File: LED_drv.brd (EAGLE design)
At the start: 160 x 100 mm, 69 parts, among them IC1 LM3409, IC2 LM393D, Q2 IPD50R380, T1 IRLR9343PBF, T2 BCX56, T4 BT169, T5 BT169, T6 TLP266J

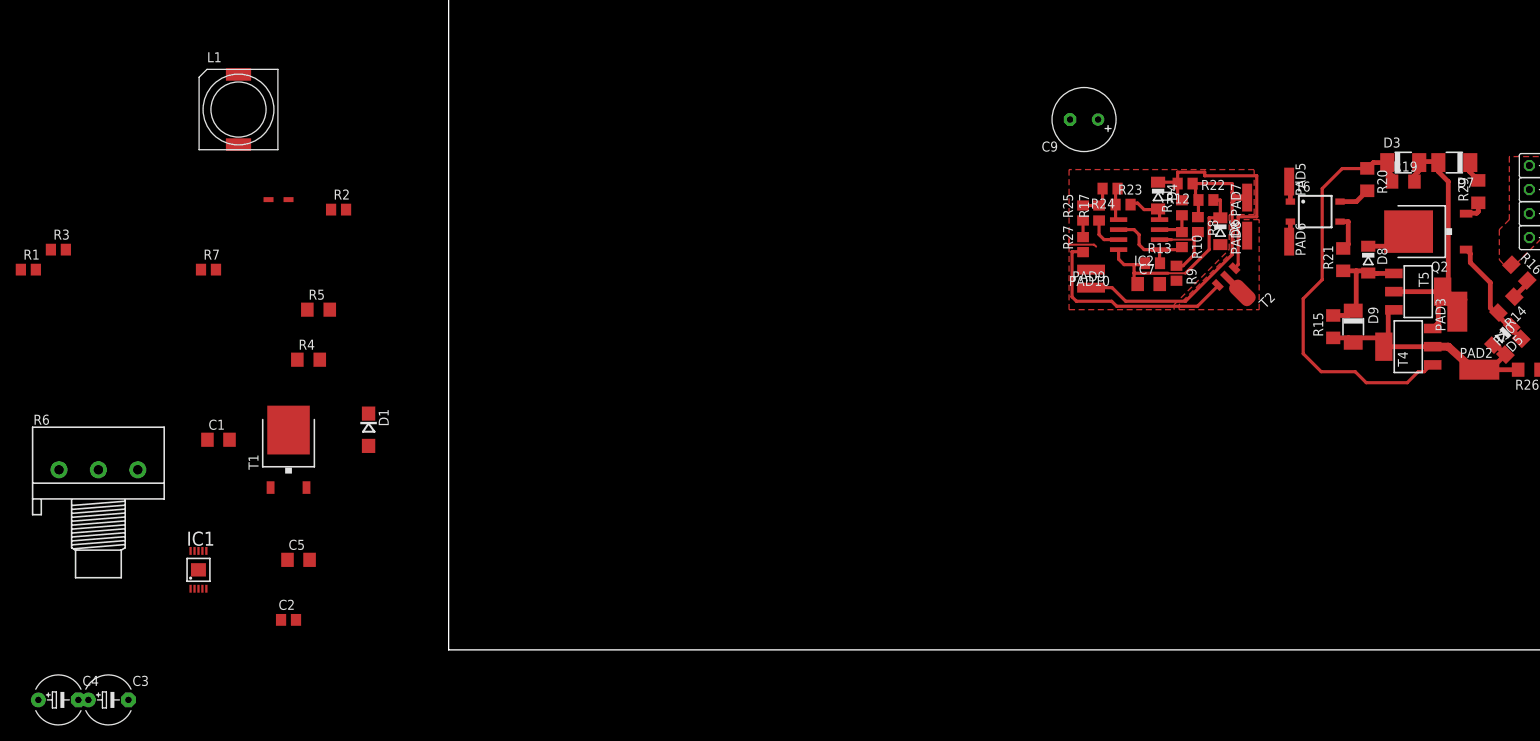
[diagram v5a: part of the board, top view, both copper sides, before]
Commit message: PCB layout complete
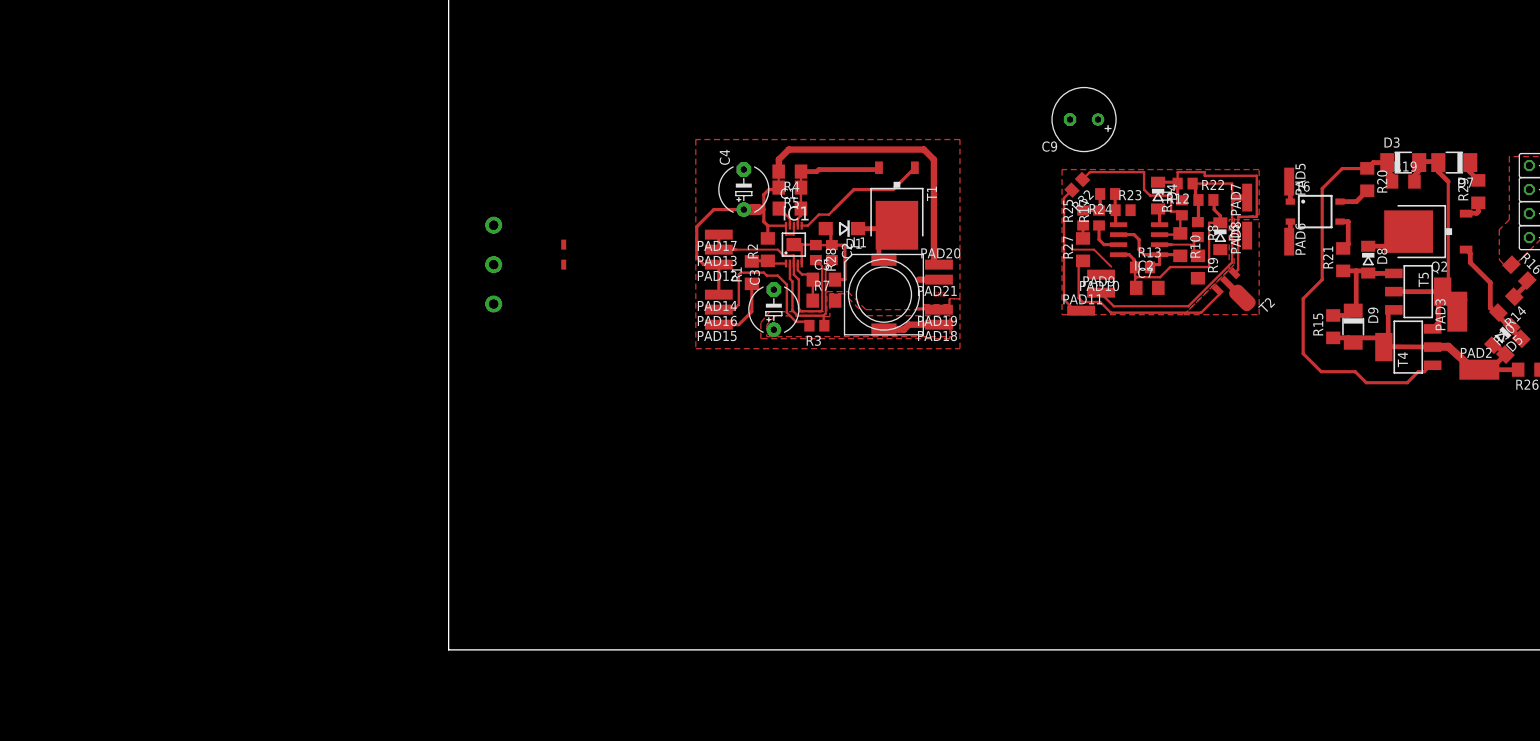
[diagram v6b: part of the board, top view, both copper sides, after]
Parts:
- added PAD11, PAD12, PAD13, PAD14, PAD15, PAD16, PAD17, PAD18, PAD19, PAD20, PAD21: (no value), wirepad:SMD1,27-2,54
- added R28: 1M, rcl:R0805
- added R32: 100k, resistor:R0805
- R1, R2, R7: device rcl:R0805 -> rcl:R1206
- R10: value 150k -> 180k; device resistor:R0805 -> rcl:R1206
- R27, R9: device resistor:R0805 -> rcl:R1206
- moved C4 108.5 mm to (37.5, 58.4), turned to 90 degrees
- moved C3 97.9 mm to (41.3, 43.2), turned to 90 degrees
- moved R3 96.7 mm to (46.7, 41.1), turned to 180 degrees
- moved R1 91.8 mm to (38.5, 47.9), turned to 90 degrees
- moved IC1 86.1 mm to (43.8, 51.4)
- moved L1 85.2 mm to (55.2, 45.1)
- moved C2 83.2 mm to (48.6, 50.4), turned to 270 degrees
- moved T1 83.2 mm to (56.9, 56.4), turned to 180 degrees
- moved C1 78.2 mm to (43.3, 56.0)
- moved R7 78.2 mm to (47.6, 44.3)
- moved C5 75.6 mm to (47.6, 47.0)
- moved R4 65.6 mm to (43.3, 60.7), turned to 180 degrees
- moved D1 65.3 mm to (49.9, 53.5), turned to 180 degrees
- moved R5 61.8 mm to (43.3, 58.7), turned to 180 degrees
- moved R6 56.5 mm to (5.71, 48.9), flipped to the bottom, turned to 90 degrees
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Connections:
- removed net N$11: IC1.3, S1.1
- removed net N$20: IC2.3, R10.1, R11.1
- new net ACTIVATION: IC1.3, PAD11.1, PAD13.1, PAD17.1, R28.2, R32.2, S1.1
- new net EER: IC2.3, R10.1, R11.1, R32.1
- net GND: now also PAD15.1, PAD19.1, PAD21.1, R28.1
- net N$10: now also PAD18.1
- net N$2: now also PAD12.1, PAD14.1, PAD20.1
- net N$8: now also PAD16.1
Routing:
- net N$2: track 0.00 -> 72.2 mm
- net ACTIVATION: track 0.00 -> 45.6 mm
- net GND: track 9.66 -> 40.7 mm
- net EER: track 0.00 -> 23.4 mm
- net N$8: track 0.00 -> 20.5 mm
- net N$5: track 0.00 -> 19.1 mm
- net N$4: track 0.00 -> 18.3 mm
- net N$9: track 0.00 -> 17.4 mm
- net N$6: track 0.00 -> 9.92 mm
- net N$10: track 0.00 -> 7.25 mm
- net N$13: track 0.00 -> 6.33 mm
- net N$20: track 5.29 -> 0.00 mm
- net N$1: track 0.00 -> 4.71 mm
- net N$3: track 0.00 -> 2.83 mm
- net N$19: track 10.3 -> 8.08 mm
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- added copper zone on layer 1, net N$10
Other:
- board text added: "GND"

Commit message: PCB layout complete
minor update
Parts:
- removed C4: 22uF/50V, rcl:E5-6
- removed C6: 100n/400V, rcl:C075-032X103
- added 0R, R31, R33, R34, R35, R36: 1R, resistor:R1206
- added C12, C13: 22uF/50V, rcl:E5-6
- added F1: (no value), fuse:SH22,5A
- added PAD22, PAD23, PAD24, PAD25, PAD26, PAD27, PAD28, PAD29: (no value), wirepad:SMD1,27-2,54
- added R37: S14K275_SMD, varistor:S14K275_SMD
- moved PAD17 36.3 mm to (68.3, 65.3)
- moved PAD19 16.9 mm to (68.3, 58.9)
- moved PAD21 15.7 mm to (68.3, 61.5)
- moved PAD20 15.7 mm to (68.3, 63.4)
- moved PAD18 6.13 mm to (68.3, 40.6)
- moved D2 5.04 mm to (146.4, 35.3), turned to 0 degrees
- moved R2 3.60 mm to (38.1, 53.5), turned to 0 degrees
- moved R30 2.98 mm to (134.7, 41.4), turned to 90 degrees
- moved R16 2.94 mm to (135.5, 50.8), turned to 270 degrees
- moved R14 2.54 mm to (134.2, 46.4), turned to 180 degrees
- moved D5 1.84 mm to (132.7, 41.4), turned to 270 degrees
- moved R26 1.30 mm to (135.9, 35.6)
- moved R18 1.22 mm to (140.9, 35.6)
- moved D1 0.84 mm to (50.7, 53.2)
- moved C2 0.51 mm to (48.6, 49.9)
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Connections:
- new net 230VAC(N/L)_IN: F1.2
- new net N$11: C13.+, C3.+, L1.2, R31.2, R33.2, R34.2, R35.2, R36.2, R7.2
- new net N$20: PAD22.1, R33.1
- new net N$32: PAD18.1, R31.1
- new net N$35: PAD23.1, R34.1
- new net N$36: PAD24.1, R35.1
- new net N$37: PAD25.1, R36.1
- net 230VAC(L/N): now also R37.2
- net 230VAC(N/L): now also F1.1, R37.1
- net ACTIVATION: now also 0R.1; no longer PAD17.1, S1.1
- net GND: now also C12.-, C13.-, PAD26.1, PAD27.1, PAD28.1, PAD29.1; no longer C4.-
- net N$10: now also 0R.2, PAD17.1, S1.1; no longer C3.+, L1.2, PAD18.1, R7.2
- net N$14: no longer C6.1
- net N$2: now also C12.+; no longer C4.+
- net N$34: no longer C6.2
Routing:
- net N$10: track 7.25 -> 33.4 mm
- net N$11: track 0.00 -> 13.3 mm
- net ACTIVATION: track 45.6 -> 55.7 mm
- net 230VAC(L/N): track 7.50 -> 15.7 mm
- net N$1: track 4.71 -> 11.4 mm
- net N$14: track 19.8 -> 25.0 mm
- net N$2: track 72.2 -> 67.8 mm
- net GND: track 40.7 -> 36.9 mm
- net 230VAC(N/L): track 36.4 -> 39.9 mm
- net N$7: track 14.9 -> 11.5 mm
- net N$37: track 0.00 -> 2.77 mm
- net N$36: track 0.00 -> 2.77 mm
- net N$35: track 0.00 -> 2.77 mm
- net N$32: track 0.00 -> 2.77 mm
- net N$20: track 0.00 -> 2.77 mm
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- added copper zone on layer 1, net N$11
- removed copper zone on layer 1, net N$10
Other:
- board text added: "ACT 42V GND"
- board text added: "LED+"
- board text added: "PR"
- board text added: "SW"
- board text removed: "GND"

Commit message: test_release
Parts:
- added D10, D11: 1n4002, diode:DO214AC
- added R38: 51k, rcl:R1206
- added R39: 86k, rcl:R1206
- added R40: 47k, rcl:R0805
- 0R: value 1R -> 0R
- R1: value (none) -> 7k5
- R2: value (none) -> 51k
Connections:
- new net N$40: PAD14.1, R39.1, R6.3
- new net N$41: D10.A, D11.C
- new net N$44: D11.A, R38.1, R39.2
- net GND: now also D10.C
- net N$2: now also R38.2; no longer PAD14.1, R6.3
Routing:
- net N$2: track 67.8 -> 64.0 mm
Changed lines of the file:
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@@
 <layer number="37" name="tTest" color="7" fill="1" visible="no" active="yes"/>
 <layer number="38" name="bTest" color="7" fill="1" visible="no" active="yes"/>
-<layer number="39" name="tKeepout" color="4" fill="11" visible="yes" active="yes"/>
-<layer number="40" name="bKeepout" color="1" fill="11" visible="yes" active="yes"/>
-<layer number="41" name="tRestrict" color="4" fill="10" visible="yes" active="yes"/>
-<layer number="42" name="bRestrict" color="1" fill="10" visible="yes" active="yes"/>
+<layer number="39" name="tKeepout" color="4" fill="11" visible="no" active="yes"/>
+<layer number="40" name="bKeepout" color="1" fill="11" visible="no" active="yes"/>
+<layer number="41" name="tRestrict" color="4" fill="10" visible="no" active="yes"/>
+<layer number="42" name="bRestrict" color="1" fill="10" visible="no" active="yes"/>
 <layer number="43" name="vRestrict" color="2" fill="10" visible="no" active="yes"/>
 <layer number="44" name="Drills" color="7" fill="1" visible="no" active="yes"/>
 <layer number="45" name="Holes" color="7" fill="1" visible="no" active="yes"/>
 <layer number="46" name="Milling" color="3" fill="1" visible="no" active="yes"/>
-<layer number="47" name="Measures" color="7" fill="1" visible="yes" active="yes"/>
-<layer number="48" name="Document" color="7" fill="1" visible="yes" active="yes"/>
+<layer number="47" name="Measures" color="7" fill="1" visible="no" active="yes"/>
+<layer number="48" name="Document" color="7" fill="1" visible="no" active="yes"/>
 <layer number="49" name="Reference" color="7" fill="1" visible="yes" active="yes"/>
 <layer number="51" name="tDocu" color="7" fill="1" visible="yes" active="yes"/>
-<layer number="52" name="bDocu" color="7" fill="1" visible="yes" active="yes"/>
+<layer number="52" name="bDocu" color="7" fill="1" visible="no" active="yes"/>
 <layer number="90" name="Modules" color="5" fill="1" visible="no" active="no"/>
 <layer number="91" name="Nets" color="2" fill="1" visible="no" active="no"/>
@@
 <element name="IC2" library="linear" package="SO08" value="LM393D" x="87.63" y="52.07" rot="R90"/>
 <element name="L1" library="miscrel" package="CDRH104-R" value="CDRH104R" x="55.245" y="45.085"/>
-<element name="R1" library="rcl" package="R1206" value="" x="38.481" y="47.879" rot="R90"/>
+<element name="R1" library="rcl" package="R1206" value="7k5" x="38.481" y="47.879" rot="R90"/>
 <element name="R10" library="rcl" package="R1206" value="180k" x="92.8624" y="51.435" rot="R270"/>
 <element name="R11" library="resistor" package="R0805" value="100k" x="93.0656" y="56.1086" rot="R90"/>
 <element name="R12" library="resistor" package="R0805" value="47k" x="93.472" y="59.182" rot="R180"/>
-<element name="R2" library="rcl" package="R1206" value="" x="38.1" y="53.467"/>
+<element name="R2" library="rcl" package="R1206" value="51k" x="38.1" y="53.467"/>
 <element name="R3" library="rcl" package="R0805" value="1k" x="46.736" y="41.148" rot="R180"/>
 <element name="R4" library="resistor" package="R1206" value="1R" x="43.307" y="60.706" rot="R180"/>
@@
 <element name="C12" library="rcl" package="E5-6" value="22uF/50V" x="49.5046" y="58.4962" rot="R270"/>
 <element name="C13" library="rcl" package="E5-6" value="22uF/50V" x="63.7032" y="56.0578" rot="R90"/>
-<element name="0R" library="resistor" package="R1206" value="1R" x="38.1" y="57.785" rot="R90"/>
+<element name="0R" library="resistor" package="R1206" value="0R" x="38.1" y="57.785" rot="R90"/>
 <element name="R37" library="varistor" package="S14K275_SMD" value="S14K275_SMD" x="142.24" y="39.8272"/>
 <element name="F1" library="fuse" package="SH22,5A" value="" x="171.45" y="45.085" rot="R90">
@@
 <attribute name="OC_FARNELL" value="unknown" x="171.45" y="45.085" size="1.778" layer="27" rot="R90" display="off"/>
 </element>
+<element name="D10" library="diode" package="DO214AC" value="1n4002" x="-4.445" y="-3.175"/>
+<element name="D11" library="diode" package="DO214AC" value="1n4002" x="-4.445" y="-9.525"/>
+<element name="R38" library="rcl" package="R1206" value="51k" x="-5.08" y="-15.875"/>
+<element name="R39" library="rcl" package="R1206" value="86k" x="-5.08" y="-22.225"/>
+<element name="R40" library="rcl" package="R0805" value="47k" x="-5.715" y="-28.575"/>
 </elements>
 <signals>
@@
 <contactref element="IC1" pad="8"/>
 <contactref element="R5" pad="2"/>
-<contactref element="R6" pad="3"/>
 <contactref element="S1" pad="2"/>
 <contactref element="PAD12" pad="1"/>
-<contactref element="PAD14" pad="1"/>
 <wire x1="42.815" y1="53.835" x2="42.815" y2="52.8574" width="0.254" layer="1"/>
 <wire x1="42.815" y1="52.8574" x2="43.815" y2="52.8574" width="0.254" layer="1"/>
@@
 <wire x1="40.005" y1="57.785" x2="40.005" y2="53.467" width="0.4064" layer="1"/>
 <wire x1="40.005" y1="53.467" x2="39.522" y2="53.467" width="0.4064" layer="1"/>
-<wire x1="34.29" y1="48.895" x2="34.29" y2="45.085" width="0.8128" layer="1"/>
 <wire x1="31.496" y1="53.721" x2="35.56" y2="57.785" width="0.4064" layer="1"/>
 <wire x1="35.56" y1="57.785" x2="40.005" y2="57.785" width="0.4064" layer="1"/>
+<contactref element="R38" pad="2"/>
 <wire x1="14.605" y1="51.435" x2="31.496" y2="49.784" width="0" layer="19" extent="1-1"/>
-<wire x1="5.715" y1="53.895" x2="14.605" y2="51.435" width="0" layer="19" extent="1-1"/>
+<wire x1="-3.658" y1="-15.875" x2="14.605" y2="51.435" width="0" layer="19" extent="1-1"/>
 </signal>
 <signal name="GND">
@@
 <wire x1="44.815" y1="50.038" x2="45.2214" y2="50.038" width="0.3048" layer="1"/>
 <wire x1="45.2214" y1="50.038" x2="45.2214" y2="50.8" width="0.3048" layer="1"/>
+<contactref element="D10" pad="C"/>
 <wire x1="68.326" y1="61.468" x2="78.867" y2="67.31" width="0" layer="19" extent="1-1"/>
 <wire x1="41.275" y1="45.72" x2="44.815" y2="49.035" width="0" layer="19" extent="1-1"/>
 <wire x1="79.121" y1="51.435" x2="68.326" y2="53.34" width="0" layer="19" extent="1-1"/>
 <wire x1="5.715" y1="43.895" x2="34.29" y2="41.275" width="0" layer="19" extent="1-1"/>
+<wire x1="-6.495" y1="-3.175" x2="5.715" y2="43.895" width="0" layer="19" extent="1-1"/>
 </signal>
 <signal name="N$4">
@@
 <contactref element="F1" pad="2"/>
 </signal>
+<signal name="N$40">
+<contactref element="R6" pad="3"/>
+<contactref element="PAD14" pad="1"/>
+<contactref element="R39" pad="1"/>
+<wire x1="5.715" y1="53.895" x2="34.29" y2="45.085" width="0" layer="19" extent="1-1"/>
+<wire x1="-6.502" y1="-22.225" x2="5.715" y2="53.895" width="0" layer="19" extent="1-1"/>
+</signal>
+<signal name="N$41">
+<contactref element="D10" pad="A"/>
+<contactref element="D11" pad="C"/>
+<wire x1="-2.395" y1="-3.175" x2="-6.495" y2="-9.525" width="0" layer="19" extent="1-1"/>
+</signal>
+<signal name="N$44">
+<contactref element="R38" pad="1"/>
+<contactref element="D11" pad="A"/>
+<contactref element="R39" pad="2"/>
+<wire x1="-6.502" y1="-15.875" x2="-3.658" y2="-22.225" width="0" layer="19" extent="1-1"/>
+<wire x1="-2.395" y1="-9.525" x2="-6.502" y2="-15.875" width="0" layer="19" extent="1-1"/>
+</signal>
 </signals>
